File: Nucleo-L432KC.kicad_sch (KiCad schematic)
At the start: 8 parts, among them U1 Nucleo_L432KC

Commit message: Schematic redesign
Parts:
- removed DS3, DS4: DCDC_PWR, Diode_SMD:D_0805_2012Metric, symbol Device:LED
- removed R2, R4: 5.1K, Resistor_SMD:R_0805_2012Metric, symbol Device:R_Small
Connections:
- net DCDC_Drive: now also U1.9 (D6); no longer U1.24 (A5)
- net Supp_Drive: now also U1.8 (D5); no longer U1.25 (A6)
- net SUPP_PWR renamed PWR
- no-connect marks 22 -> 20

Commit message: sch changes
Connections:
- net DCDC_Drive: now also U1.25 (A6); no longer U1.9 (D6)
- net DCDC_Drive2: now also U1.9 (D6); no longer U1.7 (D4)
- net Supp_Drive: now also U1.24 (A5); no longer U1.8 (D5)
- net Supp_Drive2: now also U1.8 (D5); no longer U1.6 (D3)
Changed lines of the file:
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@@
-	(wire
-		(pts
-			(xy 115.57 88.9) (xy 111.76 88.9)
-		)
-		(stroke
-			(width 0)
-			(type default)
-		)
-	)
 	(wire
 		(pts
@@
 	(wire
 		(pts
-			(xy 115.57 91.44) (xy 111.76 91.44)
-		)
-		(stroke
-			(width 0)
-			(type default)
-		)
-	)
-	(wire
-		(pts
 			(xy 152.4 82.55) (xy 152.4 81.28)
 		)
@@
 	(wire
 		(pts
+			(xy 140.97 88.9) (xy 144.78 88.9)
+		)
+		(stroke
+			(width 0)
+			(type default)
+		)
+	)
+	(wire
+		(pts
 			(xy 147.32 76.2) (xy 147.32 73.66)
+		)
+		(stroke
+			(width 0)
+			(type default)
+		)
+	)
+	(wire
+		(pts
+			(xy 140.97 91.44) (xy 144.78 91.44)
 		)
 		(stroke
@@
 		)
 	)
+	(hierarchical_label "Supp_Drive2"
+		(shape output)
+		(at 111.76 93.98 180)
+		(fields_autoplaced yes)
+		(effects
+			(font
+				(size 1.27 1.27)
+			)
+			(justify right)
+		)
+	)
 	(hierarchical_label "DCDC_PWR"
 		(shape input)
@@
 		)
 	)
+	(hierarchical_label "DCDC_Drive"
+		(shape output)
+		(at 144.78 88.9 0)
+		(fields_autoplaced yes)
+		(effects
+			(font
+				(size 1.27 1.27)
+			)
+			(justify left)
+		)
+	)
 	(hierarchical_label "DCDC_Drive2"
 		(shape output)
-		(at 111.76 91.44 180)
+		(at 111.76 96.52 180)
 		(fields_autoplaced yes)
 		(effects
@@
 		)
 	)
-	(hierarchical_label "DCDC_Drive"
-		(shape output)
-		(at 111.76 96.52 180)
-		(fields_autoplaced yes)
-		(effects
-			(font
-				(size 1.27 1.27)
-			)
-			(justify right)
-		)
-	)
 	(hierarchical_label "Supp_Drive"
 		(shape output)
-		(at 111.76 93.98 180)
-		(fields_autoplaced yes)
-		(effects
-			(font
-				(size 1.27 1.27)
-			)
-			(justify right)
-		)
-	)
-	(hierarchical_label "Supp_Drive2"
-		(shape output)
-		(at 111.76 88.9 180)
-		(fields_autoplaced yes)
-		(effects
-			(font
-				(size 1.27 1.27)
-			)
-			(justify right)
-		)
-	)
+		(at 144.78 91.44 0)
+		(fields_autoplaced yes)
+		(effects
+			(font
+				(size 1.27 1.27)
+			)
+			(justify left)
+		)
+	)

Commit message: layout changes
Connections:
- net BPS_Supp_Drive: now reaches U1.22 (A3)
- net BPS_DCDC_Drive: now reaches U1.23 (A4)
- net DCDC_Drive renamed FUSEOUT_DCDC_Drive
- net DCDC_Drive2: no longer names the net of U1.9 (D6)
- net Supp_Drive renamed FUSEOUT_Supp_Drive
- net Supp_Drive2: no longer names the net of U1.8 (D5)
- no-connect marks 20 -> 22
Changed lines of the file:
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@@
+	)
+	(junction
+		(at 108.712 83.82)
+		(diameter 0)
+		(color 0 0 0 0)
 	)
 	(junction
@@
 	)
 	(no_connect
+		(at 115.57 91.44)
+	)
+	(no_connect
 		(at 140.97 111.76)
 	)
@@
 	)
 	(no_connect
-		(at 140.97 93.98)
-	)
-	(no_connect
 		(at 140.97 81.28)
 	)
@@
 	)
 	(no_connect
-		(at 140.97 96.52)
-	)
-	(no_connect
 		(at 115.57 76.2)
 	)
@@
 	)
 	(no_connect
+		(at 115.57 88.9)
+	)
+	(no_connect
 		(at 115.57 78.74)
 	)
 	(no_connect
+		(at 115.57 93.98)
+	)
+	(no_connect
 		(at 140.97 106.68)
 	)
@@
 		(at 115.57 109.22)
 	)
+	(no_connect
+		(at 115.57 96.52)
+	)
 	(wire
 		(pts
@@
 	(wire
 		(pts
+			(xy 108.712 83.82) (xy 90.17 83.82)
+		)
+		(stroke
+			(width 0)
+			(type default)
+		)
+	)
+	(wire
+		(pts
 			(xy 161.29 114.3) (xy 161.29 116.205)
 		)
@@
 	(wire
 		(pts
-			(xy 115.57 96.52) (xy 111.76 96.52)
-		)
-		(stroke
-			(width 0)
-			(type default)
-		)
-	)
-	(wire
-		(pts
 			(xy 142.24 99.06) (xy 140.97 99.06)
 		)
@@
 	(wire
 		(pts
+			(xy 140.97 93.98) (xy 144.78 93.98)
+		)
+		(stroke
+			(width 0)
+			(type default)
+		)
+	)
+	(wire
+		(pts
+			(xy 140.97 96.52) (xy 144.78 96.52)
+		)
+		(stroke
+			(width 0)
+			(type default)
+		)
+	)
+	(wire
+		(pts
 			(xy 142.24 116.205) (xy 161.29 116.205)
 		)
@@
 	(wire
 		(pts
-			(xy 115.57 83.82) (xy 90.17 83.82)
+			(xy 115.57 83.82) (xy 108.712 83.82)
 		)
 		(stroke
@@
 		(pts
 			(xy 90.17 83.82) (xy 90.17 84.455)
-		)
-		(stroke
-			(width 0)
-			(type default)
-		)
-	)
-	(wire
-		(pts
-			(xy 115.57 93.98) (xy 111.76 93.98)
 		)
 		(stroke
@@
 		)
 	)
-	(hierarchical_label "Supp_Drive2"
-		(shape output)
-		(at 111.76 93.98 180)
-		(fields_autoplaced yes)
-		(effects
-			(font
-				(size 1.27 1.27)
-			)
-			(justify right)
-		)
-	)
 	(hierarchical_label "DCDC_PWR"
 		(shape input)
@@
 		)
 	)
-	(hierarchical_label "DCDC_Drive"
+	(hierarchical_label "BPS_DCDC_Drive"
+		(shape output)
+		(at 144.78 93.98 0)
+		(fields_autoplaced yes)
+		(effects
+			(font
+				(size 1.27 1.27)
+			)
+			(justify left)
+		)
+	)
+	(hierarchical_label "FUSEOUT_DCDC_Drive"
 		(shape output)
 		(at 144.78 88.9 0)
@@
 		)
 	)
-	(hierarchical_label "DCDC_Drive2"
+	(hierarchical_label "FUSEOUT_Supp_Drive"
 		(shape output)
-		(at 111.76 96.52 180)
+		(at 144.78 91.44 0)
 		(fields_autoplaced yes)
 		(effects
@@
 				(size 1.27 1.27)
 			)
-			(justify right)
-		)
-	)
-	(hierarchical_label "Supp_Drive"
+			(justify left)
+		)
+	)
+	(hierarchical_label "BPS_Supp_Drive"
 		(shape output)
-		(at 144.78 91.44 0)
+		(at 144.78 96.52 0)
 		(fields_autoplaced yes)
 		(effects
@@
 					(unit 1)
 				)
+			)
+		)
+	)
+	(symbol
+		(lib_id "power:PWR_FLAG")
+		(at 108.712 83.82 0)
+		(unit 1)
+		(exclude_from_sim no)
+		(in_bom yes)
+		(on_board yes)
+		(dnp no)
+		(fields_autoplaced yes)
+		(property "Reference" "#FLG01"
+			(at 108.712 81.915 0)
+			(effects
+				(font
+					(size 1.27 1.27)
+				)
+				(hide yes)
+			)
+		)
+		(property "Value" "PWR_FLAG"
+			(at 108.712 78.74 0)
+			(effects
+				(font
+					(size 1.27 1.27)
+				)
+			)
+		)
+		(property "Footprint" ""
+			(at 108.712 83.82 0)
+			(effects
+				(font
+					(size 1.27 1.27)
+				)
+				(hide yes)
+			)
+		)
+		(property "Datasheet" "~"
+			(at 108.712 83.82 0)
+			(effects
+				(font
+					(size 1.27 1.27)
+				)
+				(hide yes)
+			)
+		)
+		(property "Description" "Special symbol for telling ERC where power comes from"
+			(at 108.712 83.82 0)
+			(effects
+				(font
+					(size 1.27 1.27)
+				)
+				(hide yes)
+			)
+		)
+		(pin "1"
+		)
+		(instances
+			(project "Power-Secondary"
+				(path "/ba21eba1-72a9-489c-9498-a38516b9f252/6e50724d-fa2c-4152-a095-2c53e94da30f"
+					(reference "#FLG01")
+					(unit 1)
+				)

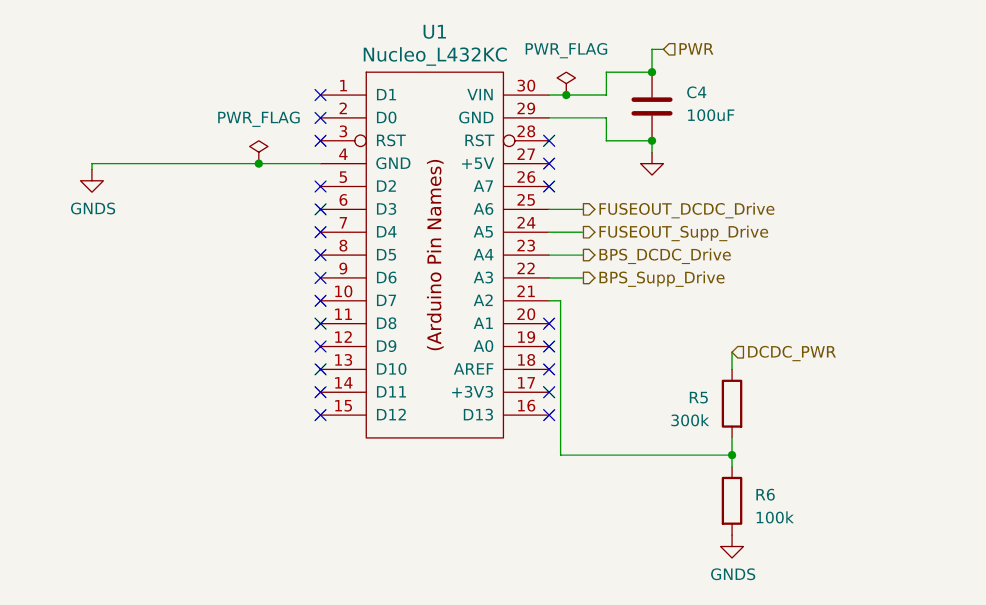
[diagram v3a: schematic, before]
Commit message: fixes to power zones
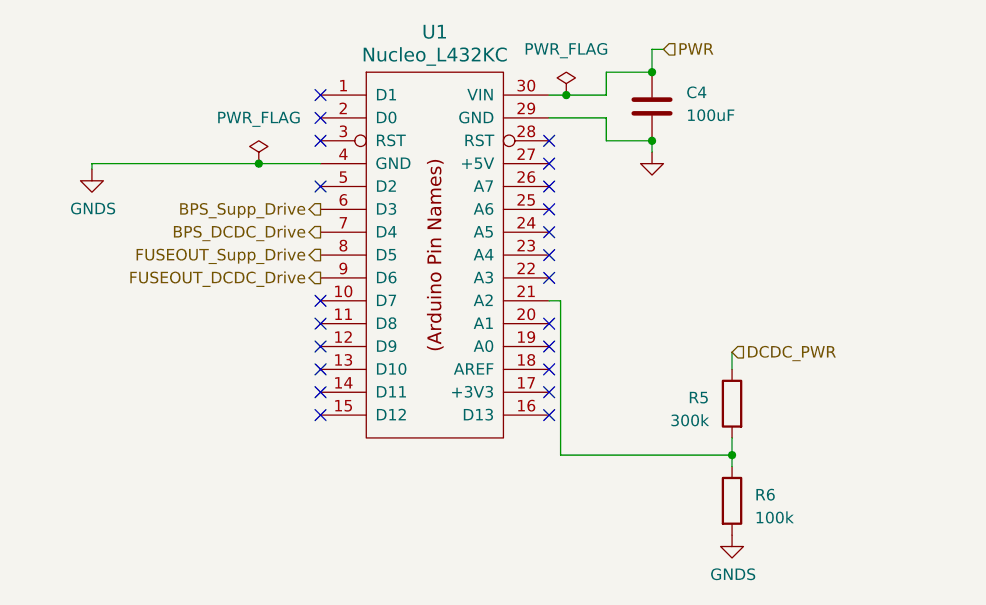
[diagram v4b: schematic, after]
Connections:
- net BPS_DCDC_Drive: now also U1.7 (D4); no longer U1.23 (A4)
- net BPS_Supp_Drive: now also U1.6 (D3); no longer U1.22 (A3)
- net FUSEOUT_DCDC_Drive: now also U1.9 (D6); no longer U1.25 (A6)
- net FUSEOUT_Supp_Drive: now also U1.8 (D5); no longer U1.24 (A5)
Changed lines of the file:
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@@
-	)
-	(no_connect
-		(at 115.57 91.44)
 	)
 	(no_connect
@@
 	)
 	(no_connect
+		(at 140.97 96.52)
+	)
+	(no_connect
 		(at 115.57 76.2)
 	)
@@
 	)
 	(no_connect
+		(at 140.97 93.98)
+	)
+	(no_connect
 		(at 115.57 99.06)
 	)
@@
 	)
 	(no_connect
-		(at 115.57 88.9)
-	)
-	(no_connect
 		(at 115.57 78.74)
 	)
 	(no_connect
-		(at 115.57 93.98)
-	)
-	(no_connect
 		(at 140.97 106.68)
 	)
@@
 	)
 	(no_connect
+		(at 140.97 91.44)
+	)
+	(no_connect
 		(at 115.57 104.14)
 	)
@@
 	)
 	(no_connect
-		(at 115.57 96.52)
+		(at 140.97 88.9)
 	)
 	(wire
@@
 	(wire
 		(pts
-			(xy 140.97 93.98) (xy 144.78 93.98)
-		)
-		(stroke
-			(width 0)
-			(type default)
-		)
-	)
-	(wire
-		(pts
-			(xy 140.97 96.52) (xy 144.78 96.52)
-		)
-		(stroke
-			(width 0)
-			(type default)
-		)
-	)
-	(wire
-		(pts
 			(xy 142.24 116.205) (xy 161.29 116.205)
 		)
@@
 	(wire
 		(pts
-			(xy 140.97 88.9) (xy 144.78 88.9)
-		)
-		(stroke
-			(width 0)
-			(type default)
-		)
-	)
-	(wire
-		(pts
 			(xy 147.32 76.2) (xy 147.32 73.66)
-		)
-		(stroke
-			(width 0)
-			(type default)
-		)
-	)
-	(wire
-		(pts
-			(xy 140.97 91.44) (xy 144.78 91.44)
 		)
 		(stroke
@@
 		)
 	)
+	(hierarchical_label "FUSEOUT_DCDC_Drive"
+		(shape output)
+		(at 115.57 96.52 180)
+		(fields_autoplaced yes)
+		(effects
+			(font
+				(size 1.27 1.27)
+			)
+			(justify right)
+		)
+	)
+	(hierarchical_label "BPS_DCDC_Drive"
+		(shape output)
+		(at 115.57 91.44 180)
+		(fields_autoplaced yes)
+		(effects
+			(font
+				(size 1.27 1.27)
+			)
+			(justify right)
+		)
+	)
 	(hierarchical_label "DCDC_PWR"
 		(shape input)
@@
 		)
 	)
-	(hierarchical_label "BPS_DCDC_Drive"
+	(hierarchical_label "BPS_Supp_Drive"
 		(shape output)
-		(at 144.78 93.98 0)
-		(fields_autoplaced yes)
-		(effects
-			(font
-				(size 1.27 1.27)
-			)
-			(justify left)
-		)
-	)
-	(hierarchical_label "FUSEOUT_DCDC_Drive"
-		(shape output)
-		(at 144.78 88.9 0)
-		(fields_autoplaced yes)
-		(effects
-			(font
-				(size 1.27 1.27)
-			)
-			(justify left)
+		(at 115.57 88.9 180)
+		(fields_autoplaced yes)
+		(effects
+			(font
+				(size 1.27 1.27)
+			)
+			(justify right)
 		)
 	)
 	(hierarchical_label "FUSEOUT_Supp_Drive"
 		(shape output)
-		(at 144.78 91.44 0)
-		(fields_autoplaced yes)
-		(effects
-			(font
-				(size 1.27 1.27)
-			)
-			(justify left)
-		)
-	)
-	(hierarchical_label "BPS_Supp_Drive"
-		(shape output)
-		(at 144.78 96.52 0)
-		(fields_autoplaced yes)
-		(effects
-			(font
-				(size 1.27 1.27)
-			)
-			(justify left)
-		)
-	)
+		(at 115.57 93.98 180)
+		(fields_autoplaced yes)
+		(effects
+			(font
+				(size 1.27 1.27)
+			)
+			(justify right)
+		)
+	)
